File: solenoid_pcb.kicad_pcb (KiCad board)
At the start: 2 copper layers, 100.1 x 33 mm, 17 parts, among them J1 VCC, J2 Programming, J3 Solenoid, Q1 IRF540NS, SW1 RESET, U1 LM2576S-3.3, U2 ESP-12F

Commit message: more tweaks
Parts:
- moved Q1 1.60 mm to (127.3, 51.2)
- moved R4 1.00 mm to (109.1, 57.1)
- moved R3 0.90 mm to (109.1, 61.7)
- moved C1 0.50 mm to (72.9, 45.0)
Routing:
- net Net-(D2-Pad2): track 13.6 -> 12.3 mm
- net Net-(Q1-Pad1): track 22.0 -> 23.1 mm
- net GND: track 40.2 -> 39.3 mm, vias 83 -> 82
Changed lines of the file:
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@@
     (thickness 1.6)
     (drawings 14)
-    (tracks 186)
+    (tracks 183)
     (zones 0)
     (modules 17)
@@
   (page A4)
   (layers
-    (0 F.Cu signal)
-    (31 B.Cu signal)
+    (0 F.Cu signal hide)
+    (31 B.Cu signal hide)
     (32 B.Adhes user)
     (33 F.Adhes user)
@@
   )
   (module Capacitor_SMD:CP_Elec_6.3x5.4 (layer F.Cu)
-    (at 72.4 45)
+    (at 72.9 45)
     (descr "SMD capacitor, aluminum electrolytic, Panasonic C55, 6.3x5.4mm")
     (tags "capacitor electrolytic")
@@
   )
   (module Resistor_SMD:R_0805_2012Metric_Pad1.15x1.40mm_HandSolder (layer F.Cu)
-    (at 109 58.1 270)
+    (at 109.1 57.1 270)
     (descr "Resistor SMD 0805 (2012 Metric), square (rectangular) end terminal, IPC_7351 nominal with elongated pad for handsoldering. (Body size source: https://docs.google.com/spreadsheets/d/1BsfQQcO9C6DZCsRaXUlFlo91Tg2WpOkGARC1WS5S8t0/edit?usp=sharing), generated with kicad-footprint-generator")
     (tags "resistor handsolder")
@@
   )
   (module Resistor_SMD:R_0805_2012Metric_Pad1.15x1.40mm_HandSolder (layer F.Cu)
-    (at 109.1 62.6 270)
+    (at 109.1 61.7 270)
     (descr "Resistor SMD 0805 (2012 Metric), square (rectangular) end terminal, IPC_7351 nominal with elongated pad for handsoldering. (Body size source: https://docs.google.com/spreadsheets/d/1BsfQQcO9C6DZCsRaXUlFlo91Tg2WpOkGARC1WS5S8t0/edit?usp=sharing), generated with kicad-footprint-generator")
     (tags "resistor handsolder")
@@
   )
   (module Package_TO_SOT_SMD:TO-263-2 (layer F.Cu)
-    (at 127.4 52.8 90)
+    (at 127.3 51.2 90)
     (descr "TO-263 / D2PAK / DDPAK SMD package, http://www.infineon.com/cms/en/product/packages/PG-TO263/PG-TO263-3-1/")
     (tags "D2PAK DDPAK TO-263 D2PAK-3 TO-263-3 SOT-404")
@@
   (segment (start 104 70.6) (end 104 64.5) (width 0.4) (layer B.Cu) (net 1))
   (segment (start 104 64.4) (end 104.025 64.425) (width 0.4) (layer F.Cu) (net 1))
-  (segment (start 104.775 63.625) (end 109.1 63.625) (width 0.4) (layer F.Cu) (net 1))
-  (segment (start 104 64.4) (end 104.775 63.625) (width 0.4) (layer F.Cu) (net 1))
-  (segment (start 109.8 63.625) (end 109.825 63.6) (width 0.25) (layer F.Cu) (net 1))
-  (segment (start 109.1 63.625) (end 109.8 63.625) (width 0.25) (layer F.Cu) (net 1))
-  (via (at 111.1 63.6) (size 0.8) (drill 0.4) (layers F.Cu B.Cu) (net 1))
-  (segment (start 109.825 63.6) (end 111.1 63.6) (width 0.25) (layer F.Cu) (net 1))
   (segment (start 70.5 53.25) (end 70.5 55) (width 0.25) (layer F.Cu) (net 1))
   (segment (start 84.5 43.7) (end 81.5 43.7) (width 0.4) (layer F.Cu) (net 1))
@@
   (segment (start 72.65 53.25) (end 72.7 53.3) (width 0.4) (layer F.Cu) (net 1))
   (segment (start 70.5 53.25) (end 72.65 53.25) (width 0.4) (layer F.Cu) (net 1))
-  (via (at 74.1 46.7) (size 0.8) (drill 0.4) (layers F.Cu B.Cu) (net 1))
-  (segment (start 75.2 45.6) (end 74.1 46.7) (width 0.4) (layer F.Cu) (net 1))
-  (segment (start 75.2 45) (end 75.2 45.6) (width 0.4) (layer F.Cu) (net 1))
   (via (at 80.1 53.4) (size 0.8) (drill 0.4) (layers F.Cu B.Cu) (net 1))
   (segment (start 77.4 53.4) (end 80.1 53.4) (width 0.4) (layer F.Cu) (net 1))
+  (segment (start 75.7 45.8) (end 74.2 47.3) (width 0.4) (layer F.Cu) (net 1))
+  (via (at 74.2 47.3) (size 0.8) (drill 0.4) (layers F.Cu B.Cu) (net 1))
+  (segment (start 75.7 45) (end 75.7 45.8) (width 0.4) (layer F.Cu) (net 1))
+  (segment (start 104 64.4) (end 105.7 64.4) (width 0.4) (layer F.Cu) (net 1))
+  (segment (start 107.375 62.725) (end 109.1 62.725) (width 0.4) (layer F.Cu) (net 1))
+  (segment (start 105.7 64.4) (end 107.375 62.725) (width 0.4) (layer F.Cu) (net 1))
   (segment (start 64.2 53.05) (end 64.2 55.525) (width 0.4) (layer F.Cu) (net 2))
   (segment (start 62.45 51.3) (end 64.2 53.05) (width 0.4) (layer F.Cu) (net 2))
@@
   (segment (start 85.5 65.425) (end 85.5 67.142476) (width 0.25) (layer F.Cu) (net 5))
   (segment (start 104 62.4) (end 104.025 62.375) (width 0.25) (layer F.Cu) (net 6))
-  (segment (start 104.825 61.575) (end 109.1 61.575) (width 0.25) (layer F.Cu) (net 6))
-  (segment (start 104 62.4) (end 104.825 61.575) (width 0.25) (layer F.Cu) (net 6))
+  (segment (start 108.4 60.675) (end 109.1 60.675) (width 0.25) (layer F.Cu) (net 6))
+  (segment (start 106.675 62.4) (end 108.4 60.675) (width 0.25) (layer F.Cu) (net 6))
+  (segment (start 104 62.4) (end 106.675 62.4) (width 0.25) (layer F.Cu) (net 6))
   (segment (start 97.11499 57.28501) (end 104 50.4) (width 0.25) (layer F.Cu) (net 7))
   (segment (start 97.11499 67.28501) (end 97.11499 57.28501) (width 0.25) (layer F.Cu) (net 7))
@@
   (segment (start 118.55 47) (end 119.2 47.65) (width 0.4) (layer F.Cu) (net 9))
   (segment (start 115.3 47) (end 118.55 47) (width 0.4) (layer F.Cu) (net 9))
-  (segment (start 119.2 48.5) (end 119.2 47.65) (width 0.4) (layer F.Cu) (net 9))
-  (segment (start 120.125 49.425) (end 119.2 48.5) (width 0.4) (layer F.Cu) (net 9))
-  (segment (start 127.4 49.425) (end 120.125 49.425) (width 0.4) (layer F.Cu) (net 9))
-  (segment (start 123.36 57.075) (end 124.86 58.575) (width 0.4) (layer F.Cu) (net 10))
-  (segment (start 109 57.075) (end 123.36 57.075) (width 0.4) (layer F.Cu) (net 10))
-  (segment (start 124.675 58.76) (end 124.86 58.575) (width 0.4) (layer F.Cu) (net 10))
-  (segment (start 124.675 64) (end 124.675 58.76) (width 0.4) (layer F.Cu) (net 10))
-  (segment (start 109 59.7) (end 109 59.125) (width 0.25) (layer F.Cu) (net 11))
-  (segment (start 108.3 60.4) (end 109 59.7) (width 0.25) (layer F.Cu) (net 11))
-  (segment (start 104 60.4) (end 108.3 60.4) (width 0.25) (layer F.Cu) (net 11))
+  (segment (start 127.125 47.65) (end 127.3 47.825) (width 0.4) (layer F.Cu) (net 9))
+  (segment (start 119.2 47.65) (end 127.125 47.65) (width 0.4) (layer F.Cu) (net 9))
+  (segment (start 123.86 56.075) (end 124.76 56.975) (width 0.25) (layer F.Cu) (net 10))
+  (segment (start 109.1 56.075) (end 123.86 56.075) (width 0.25) (layer F.Cu) (net 10))
+  (segment (start 124.76 63.915) (end 124.675 64) (width 0.25) (layer F.Cu) (net 10))
+  (segment (start 124.76 56.975) (end 124.76 63.915) (width 0.25) (layer F.Cu) (net 10))
+  (segment (start 104 60.4) (end 105.3 60.4) (width 0.25) (layer F.Cu) (net 11))
+  (segment (start 107.575 58.125) (end 109.1 58.125) (width 0.25) (layer F.Cu) (net 11))
+  (segment (start 105.3 60.4) (end 107.575 58.125) (width 0.25) (layer F.Cu) (net 11))
   (segment (start 118.55 45) (end 119.2 44.35) (width 0.4) (layer F.Cu) (net 12))
   (segment (start 115.3 45) (end 118.55 45) (width 0.4) (layer F.Cu) (net 12))

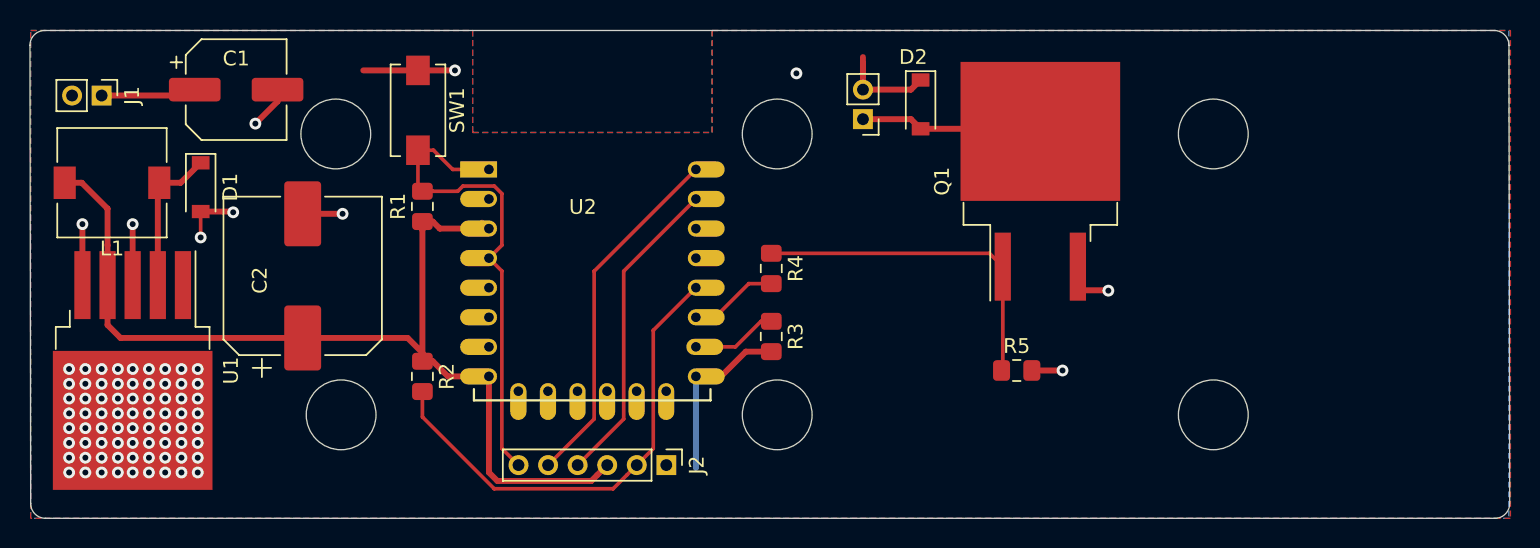
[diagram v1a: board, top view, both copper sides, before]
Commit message: Dingen en zaken
3.3v heeft een eigen power symbol (ipv global label)
`sig` label locla gemaakt, kleinigheidje
2mm header is niet standaard! (2,54mm / 100mil wel)
Ook ff normale run-off-the-mill 6mm switch erin gestopt
Alle headers staan nu op het zelfde 2.54mm grid
Weet je zeker dat de footprint van je inductor klopt?
Zou je batterij input naast je dikke tor zetten, nu gaan je pulsen over je hele powerplane
Waarom eigen lijk over je hele board een powerplane op 12V, terwijl dat alleen door je fet gebruikt wordt?
Waar zijn die 6 gaten eigenlijk voor in't bordje? Schroeven zijn vaak groter zijn dan je denkt.. ;)
Heb ze er voor 't gemak ff uit gegooid, maar kunnen terug natuurlijk.
Verder nog wat via stiches erin stampen en wellicht nog wat decouple caps rond je ESP.
Enneuh.. ook handig (als 't een devbord is) om wat meer IO's richting header te voeren.. (ledje, input knoppies of miss zelfs een klein displaytje ofzo?)

ESP12 dingen:
Ben geswitched naar de stock (kicad) ESP12 symbol (git submodule lijkt te missen en is dus niet nodig)
Jouw ESP12 footprint is ook double sided, dat lijkt me nie zo handig.. Stock komponent lost ook dit op.
Weerstanden op GPIO0 en 15 volgens mij voor het booten/programmen van de ESP8266 dingetje?
GPIO02 moet je dacht ik naar vcc pullen, dus zou men solenoid ergens anders aan hangen.
GPIO16 aan reset, is dat een truuk om een software reset te doen? GPIO16 heeft een interne pull
down, dus weet niet offie dan lekker wil booten als je die aan RST hangt..
Anyway.. ken de ESP8266 niet zo goed, dus check vooral ff.. :) (Waarom eigenlijk niet 'n ESP32?)
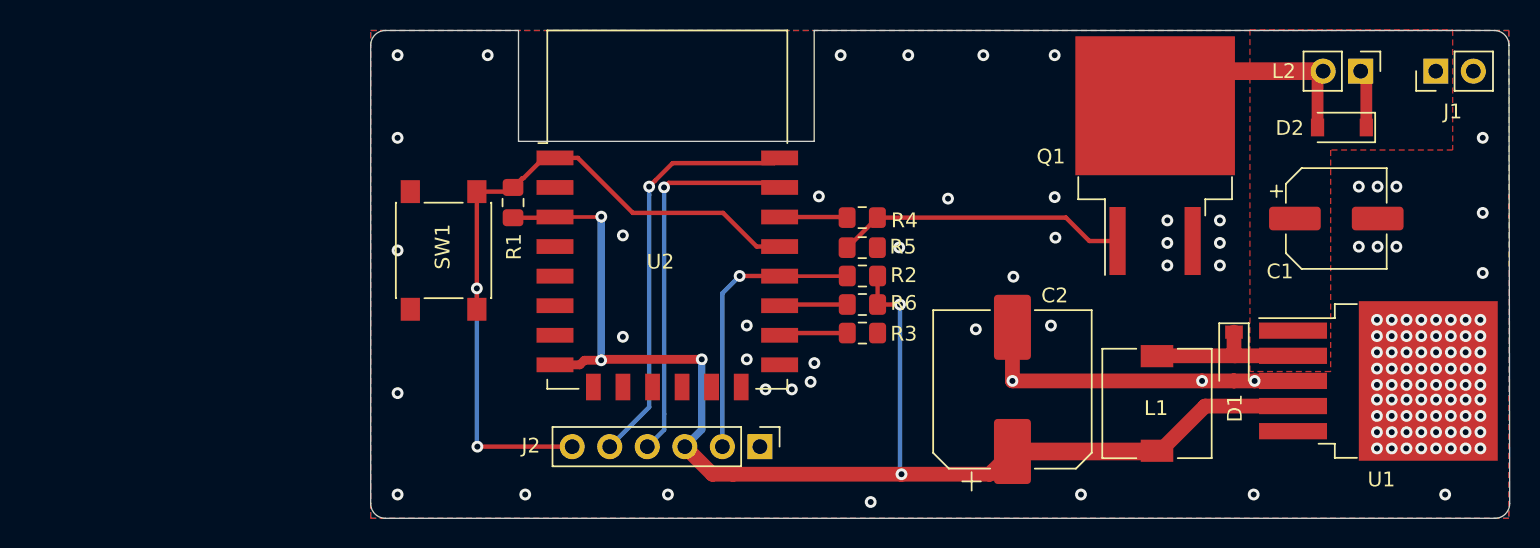
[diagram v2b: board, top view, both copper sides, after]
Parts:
- removed J3: Solenoid, Connector_PinHeader_2.00mm:PinHeader_1x02_P2.00mm_Vertical
- added L2: Solenoid, Connector_PinHeader_2.54mm:PinHeader_1x02_P2.54mm_Vertical, F.Cu at (149.0, 43.8)
- added R6: 10K, Resistor_SMD:R_0805_2012Metric_Pad1.15x1.40mm_HandSolder, F.Cu at (115.3, 59.5)
- J1: value VCC -> Power; footprint Connector_PinHeader_2.00mm:PinHeader_1x02_P2.00mm_Vertical -> Connector_PinHeader_2.54mm:PinHeader_1x02_P2.54mm_Vertical
- J2: footprint Connector_PinHeader_2.00mm:PinHeader_1x06_P2.00mm_Vertical -> Connector_PinHeader_2.54mm:PinHeader_1x06_P2.54mm_Vertical
- SW1: footprint Button_Switch_SMD:SW_SPST_EVQPE1 -> Button_Switch_SMD:SW_SPST_PTS645
- U2: footprint ESP8266:ESP-12E -> RF_Module:ESP-12E
- moved J1 90.3 mm to (154.1, 43.8), turned to 90 degrees
- moved U1 84.3 mm to (150.2, 64.7), turned to 0 degrees
- moved C1 74.9 mm to (147.3, 53.7)
- moved L1 72.3 mm to (135.2, 66.2), turned to 270 degrees
- moved D1 70.8 mm to (140.4, 63.1)
- moved C2 48.6 mm to (125.4, 65.3)
- moved R2 30.5 mm to (115.3, 57.6), turned to 180 degrees
- moved D2 28.5 mm to (147.7, 47.6), turned to 180 degrees
- moved R5 13.3 mm to (115.3, 55.7)
- moved U2 12.4 mm to (102.1, 53.1)
- moved SW1 9.64 mm to (86.9, 55.9), turned to 90 degrees
- moved Q1 7.96 mm to (135.1, 49.5)
- moved R4 7.05 mm to (115.3, 53.7), turned to 180 degrees
- moved J2 6.45 mm to (108.3, 69.2)
- moved R3 6.17 mm to (115.3, 61.5), turned to 0 degrees
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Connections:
- net +3.3V renamed +3V3
- net VCC renamed +12V
- J2 pad 6: /RST -> /~RST
- R1 pad 2: /RST -> /~RST
- R4 pad 2: SIG -> /SIG
- SW1 pad 2: /RST -> /~RST
- U2 pad 1: /RST -> /~RST
- U2 pad 10: Net-(R3-Pad1) -> Net-(U2-Pad10)
- U2 pad 11: SIG -> Net-(U2-Pad11)
- U2 pad 12: /GPIO0 -> Net-(U2-Pad12)
- U2 pad 13: (no net) -> Net-(U2-Pad13)
- U2 pad 14: (no net) -> Net-(U2-Pad14)
- U2 pad 15: /RXD -> GND
- U2 pad 16: /TXD -> Net-(R3-Pad1)
- U2 pad 17: (no net) -> Net-(R6-Pad2)
- U2 pad 18: (no net) -> /GPIO0
- U2 pad 19: (no net) -> /~RST
- U2 pad 2: (no net) -> Net-(U2-Pad2)
- U2 pad 20: (no net) -> /SIG
- U2 pad 21: (no net) -> /RXD
- U2 pad 22: (no net) -> /TXD
- U2 pad 4: /RST -> Net-(U2-Pad4)
- U2 pad 5: (no net) -> Net-(U2-Pad5)
- U2 pad 6: (no net) -> Net-(U2-Pad6)
- U2 pad 7: (no net) -> Net-(U2-Pad7)
- U2 pad 9: GND -> Net-(U2-Pad9)
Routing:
- net /~RST: track 0.00 -> 49.0 mm, vias 0 -> 2
- net /RST: track 34.2 -> 0.00 mm
- net GND: track 39.3 -> 22.6 mm, vias 82 -> 122
- net +3V3: track 74.5 -> 91.0 mm, vias 0 -> 5
- net /GPIO0: track 32.5 -> 19.4 mm, vias 0 -> 1
- net +12V: track 13.2 -> 3.97 mm
- net Net-(D2-Pad2): track 12.3 -> 20.7 mm
- net SIG: track 6.04 -> 0.00 mm
- net /RXD: track 21.3 -> 26.1 mm, vias 0 -> 1
- net Net-(R6-Pad2): track 0.00 -> 4.61 mm
- net /SIG: track 0.00 -> 4.58 mm
- net /TXD: track 24.1 -> 28.3 mm, vias 0 -> 1
- net Net-(Q1-Pad1): track 23.1 -> 19.8 mm
- net Net-(R3-Pad1): track 5.85 -> 4.64 mm
- net Net-(D1-Pad1): track 10.3 -> 10.8 mm
- added copper zone on F.Cu, net GND
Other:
- board size 100.1 x 33 mm -> 77.1 x 33 mm

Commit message: Create smaller board, components to back (except ESP12), 2 channel output
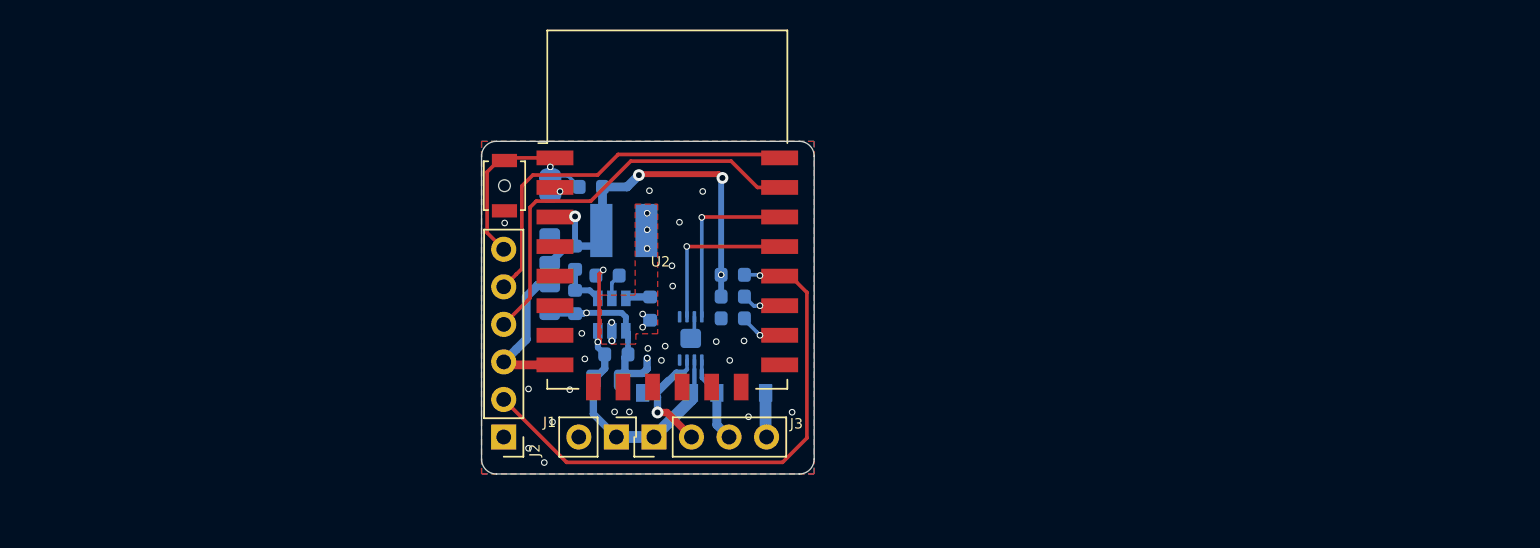
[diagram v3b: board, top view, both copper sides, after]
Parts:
- removed L2: Solenoid, Connector_PinHeader_2.54mm:PinHeader_1x02_P2.54mm_Vertical
- removed Q1: IRF540NS, Package_TO_SOT_SMD:TO-263-2
- added C3: 22u, Capacitor_SMD:C_0805_2012Metric, B.Cu at (94.1, 59.2)
- added C4: 22u, Capacitor_SMD:C_0805_2012Metric, B.Cu at (98.0, 64.6)
- added C5: 100n, Capacitor_SMD:C_0603_1608Metric, B.Cu at (98.6, 62.9)
- added J3: Solenoid, Connector_PinHeader_2.54mm:PinHeader_1x04_P2.54mm_Vertical, F.Cu at (101.2, 68.5)
- added JP1: Jumper, Jumper:SolderJumper-2_P1.3mm_Open_RoundedPad1.0x1.5mm, B.Cu at (94.1, 51.5)
- added R7: 33.2k, Resistor_SMD:R_0603_1608Metric, B.Cu at (95.8, 56.4)
- added U3: MCP14A0305xMNY, Package_DFN_QFN:WDFN-8-1EP_3x2mm_P0.5mm_EP1.3x1.4mm, B.Cu at (103.6, 61.8)
- C1: value 100u -> 100n; footprint Capacitor_SMD:CP_Elec_6.3x5.4 -> Capacitor_SMD:C_0603_1608Metric; moved to B.Cu
- C2: value 1000u -> 22u; footprint Capacitor_SMD:CP_Elec_10x10.5 -> Capacitor_SMD:C_0805_2012Metric; moved to B.Cu
- D1: value MBR0530 -> 1N4148W; moved to B.Cu
- D2: moved to B.Cu
- J2: value Programming -> PGM
- L1: value 100u -> 2.2u / 2Amp; footprint Inductor_SMD:L_7.3x7.3_H4.5 -> Inductor_SMD:L_Bourns-SRN4018; moved to B.Cu
- R1, R2, R3, R5, R6: footprint Resistor_SMD:R_0805_2012Metric_Pad1.15x1.40mm_HandSolder -> Resistor_SMD:R_0603_1608Metric; moved to B.Cu
- R4: value 470 -> 10K; footprint Resistor_SMD:R_0805_2012Metric_Pad1.15x1.40mm_HandSolder -> Resistor_SMD:R_0603_1608Metric; moved to B.Cu
- SW1: footprint Button_Switch_SMD:SW_SPST_PTS645 -> Button_Switch_SMD:SW_SPST_B3U-1000P-B
- U1: value LM2576S-3.3 -> TPS561201; footprint Package_TO_SOT_SMD:TO-263-5_TabPin3 -> Package_TO_SOT_SMD:SOT-23-6; moved to B.Cu
- moved J1 60.7 mm to (98.6, 68.5), turned to 270 degrees
- moved U1 52.0 mm to (98.3, 60.2), turned to 90 degrees
- moved C1 46.8 mm to (100.9, 59.8), turned to 90 degrees
- moved D2 44.4 mm to (107.1, 65.5), turned to 0 degrees
- moved D1 38.4 mm to (102.0, 65.5), turned to 180 degrees
- moved L1 37.9 mm to (99.1, 54.5), turned to 180 degrees
- moved C2 32.7 mm to (94.1, 55.8)
- moved R5 19.8 mm to (95.8, 59.4), turned to 270 degrees
- moved R4 17.7 mm to (98.0, 57.6)
- moved J2 17.3 mm to (91.0, 68.5), turned to 180 degrees
- moved R3 8.83 mm to (106.5, 60.5), turned to 180 degrees
- moved R6 8.79 mm to (106.5, 59.0), turned to 0 degrees
- moved R2 8.77 mm to (106.5, 57.5), turned to 0 degrees
- moved SW1 6.01 mm to (91.1, 51.5)
- moved R1 5.37 mm to (96.9, 51.6), turned to 180 degrees
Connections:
- C1 pad 1: +12V -> Net-(C1-Pad1)
- C1 pad 2: GND -> Net-(C1-Pad2)
- D1 pad 1: Net-(D1-Pad1) -> +12V
- D1 pad 2: GND -> /~OUT_A
- D2 pad 1: +12V -> /OUT_B
- D2 pad 2: Net-(D2-Pad2) -> GND
- L1 pad 1: Net-(D1-Pad1) -> Net-(C1-Pad1)
- R4 pad 1: Net-(Q1-Pad1) -> Net-(R4-Pad1)
- R4 pad 2: /SIG -> +12V
- R5 pad 1: Net-(Q1-Pad1) -> Net-(R5-Pad1)
- U1 pad 1: +12V -> GND
- U1 pad 2: Net-(D1-Pad1) -> Net-(C1-Pad1)
- U1 pad 3: GND -> +12V
- U1 pad 4: +3V3 -> Net-(R5-Pad1)
- U1 pad 5: GND -> Net-(R4-Pad1)
- U2 pad 19: /~RST -> /CHN_A
- U2 pad 20: /SIG -> /CHN_B
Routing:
- net +3V3: track 91.0 -> 40.0 mm, vias 5 -> 4
- net /~RST: track 49.0 -> 14.3 mm, vias 2 -> 1
- net Net-(D2-Pad2): track 20.7 -> 0.00 mm
- net Net-(Q1-Pad1): track 19.8 -> 0.00 mm
- net /GPIO0: track 19.4 -> 38.9 mm
- net +12V: track 3.97 -> 22.9 mm, vias 0 -> 2
- net /CHN_B: track 0.00 -> 12.0 mm, vias 0 -> 1
- net /~OUT_A: track 0.00 -> 11.5 mm, vias 0 -> 1
- net /CHN_A: track 0.00 -> 11.1 mm, vias 0 -> 1
- net Net-(D1-Pad1): track 10.8 -> 0.00 mm
- net /OUT_B: track 0.00 -> 5.97 mm
- net GND: track 22.6 -> 17.4 mm, vias 122 -> 25
- net /SIG: track 4.58 -> 0.00 mm
- net Net-(C1-Pad1): track 0.00 -> 3.31 mm, vias 0 -> 7
- net Net-(R5-Pad1): track 0.00 -> 3.18 mm
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- added copper zone on F.Cu, net Net-(C1-Pad1)
- removed copper zone on F.Cu, net +12V
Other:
- board size 77.1 x 33 mm -> 22.5 x 22.5 mm
